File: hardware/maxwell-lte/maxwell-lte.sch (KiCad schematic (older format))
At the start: 25 parts, among them J1 LTE, J2 GPS, J3 Input, J4 SIM_Card, U1 MIC5209-ADJ, U2 SIM7000A, U3 TXB0104D, U4 SC16IS750IPW, Y1 Crystal

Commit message: Rev 1.1.
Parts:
- removed C8, C9: 220u / TAJC227K006RNJ, coddingtonbear:CP_Tantalum_Case-C_EIA-6032-28_Milling, symbol Device:CP
- removed R4, R5, R6: 22, coddingtonbear:0805_Milling, symbol Device:R
- added D1: 1N4148W, coddingtonbear:D_SOD-123_LargePads, symbol Device:D
- added R7: 1k, coddingtonbear:0805_Milling, symbol Device:R
- added R8: 3.6k, coddingtonbear:0805_Milling, symbol Device:R
- C7: value 220u / TAJC227K006RNJ -> 0.1 / FG0H104ZF; footprint coddingtonbear:CP_Tantalum_Case-C_EIA-6032-28_Milling -> Capacitor_THT:C_Disc_D11.0mm_W5.0mm_P5.00mm
- J1, J2: footprint Connector_Coaxial:SMA_Amphenol_132134_Vertical -> coddingtonbear:SMA_Amphenol_132134_Vertical_Largepads
- U1: footprint Package_SO:SOIC-8_3.9x4.9mm_P1.27mm -> coddingtonbear:SOIC-8_3.9x4.9mm_P1.27mm_LargePads
- U3: footprint Package_SO:SOIC-14_3.9x8.7mm_P1.27mm -> coddingtonbear:SOIC-14_3.9x8.7mm_P1.27mm_LargePads
- U4: footprint Package_SO:TSSOP-24_4.4x7.8mm_P0.65mm -> coddingtonbear:TSSOP-24_4.4x7.8mm_P0.65mm_LargePads
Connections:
- net +3V3: now also R7.1
- net GND: now also R8.2
- net EN_OUTPUT: now reaches U4.21 (DTRA/)
- net EN_OUTPUT: now also U3.8 (OE)
- net at U2.31 (SIM_DATA): now also J4.7 (I/O)
- net at U2.32 (SIM_CLK): now also J4.3 (CLK)
- net at U2.33 (SIM_RST): now also J4.2 (RST)
- net VDD_EXT renamed +1V8
- net +1V8: now also D1.1 (K); no longer U3.8 (OE)
- new net: D1.2 (A), R7.2, R8.1
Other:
- moved on the sheet: J1
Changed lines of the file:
@@
 EESchema Schematic File Version 4
 LIBS:maxwell-lte-cache
-EELAYER 26 0
+EELAYER 28 0
 EELAYER END
 $Descr A4 11693 8268
@@
 L Connector:Conn_Coaxial J1
 U 1 1 5BB94EB6
-P 1900 1750
-F 0 "J1" H 2000 1634 50  0000 L CNN
-F 1 "LTE" H 2000 1725 50  0000 L CNN
-F 2 "Connector_Coaxial:SMA_Amphenol_132134_Vertical" H 1900 1750 50  0001 C CNN
-F 3 " ~" H 1900 1750 50  0001 C CNN
-	1    1900 1750
+P 1850 1400
+F 0 "J1" H 1950 1284 50  0000 L CNN
+F 1 "LTE" H 1950 1375 50  0000 L CNN
+F 2 "coddingtonbear:SMA_Amphenol_132134_Vertical_Largepads" H 1850 1400 50  0001 C CNN
+F 3 " ~" H 1850 1400 50  0001 C CNN
+	1    1850 1400
 	-1   0    0    1
 $EndComp
@@
 F 0 "J2" H 2000 2184 50  0000 L CNN
 F 1 "GPS" H 2000 2275 50  0000 L CNN
-F 2 "Connector_Coaxial:SMA_Amphenol_132134_Vertical" H 1900 2300 50  0001 C CNN
+F 2 "coddingtonbear:SMA_Amphenol_132134_Vertical_Largepads" H 1900 2300 50  0001 C CNN
 F 3 " ~" H 1900 2300 50  0001 C CNN
 	1    1900 2300
@@
 	1    0    0    -1
 $EndComp
-Wire Wire Line
-	2100 1750 3600 1750
-Wire Wire Line
-	3600 1750 3600 2350
-Wire Wire Line
-	2100 2300 3500 2300
 Wire Wire Line
 	3500 2300 3500 2350
@@
 F 0 "U4" H 9200 1413 60  0000 C CNN
 F 1 "SC16IS750IPW" H 9200 1519 60  0000 C CNN
-F 2 "Package_SO:TSSOP-24_4.4x7.8mm_P0.65mm" H 9200 3550 60  0001 C CNN
+F 2 "coddingtonbear:TSSOP-24_4.4x7.8mm_P0.65mm_LargePads" H 9200 3550 60  0001 C CNN
 F 3 "" H 9200 3550 60  0000 C CNN
 	1    9200 2600
@@
 F 0 "U3" H 7450 2264 50  0000 C CNN
 F 1 "TXB0104D" H 7150 2350 50  0000 C CNN
-F 2 "Package_SO:SOIC-14_3.9x8.7mm_P1.27mm" H 7450 2300 50  0001 C CNN
+F 2 "coddingtonbear:SOIC-14_3.9x8.7mm_P1.27mm_LargePads" H 7450 2300 50  0001 C CNN
 F 3 "http://www.ti.com/lit/ds/symlink/txb0104.pdf" H 7560 3145 50  0001 C CNN
 	1    7450 3050
@@
 F 0 "U1" H 3300 6887 60  0000 C CNN
 F 1 "MIC5209-ADJ" H 3300 6781 60  0000 C CNN
-F 2 "Package_SO:SOIC-8_3.9x4.9mm_P1.27mm" H 3300 6400 60  0001 C CNN
+F 2 "coddingtonbear:SOIC-8_3.9x4.9mm_P1.27mm_LargePads" H 3300 6400 60  0001 C CNN
 F 3 "" H 3300 6400 60  0001 C CNN
 	1    3300 6400
@@
 $EndComp
 Wire Wire Line
-	4800 2350 4800 1850
-Wire Wire Line
-	4800 1850 6450 1850
-Wire Wire Line
-	7350 1850 7350 2250
-Wire Wire Line
 	7350 2250 7350 2350
-Connection ~ 7350 2250
 Wire Wire Line
 	7550 2250 7550 2350
@@
 L power:GND #PWR0117
 U 1 1 5BBEDF0C
-P 1400 1550
-F 0 "#PWR0117" H 1400 1300 50  0001 C CNN
-F 1 "GND" H 1405 1377 50  0000 C CNN
-F 2 "" H 1400 1550 50  0001 C CNN
-F 3 "" H 1400 1550 50  0001 C CNN
-	1    1400 1550
+P 1350 1200
+F 0 "#PWR0117" H 1350 950 50  0001 C CNN
+F 1 "GND" H 1355 1027 50  0000 C CNN
+F 2 "" H 1350 1200 50  0001 C CNN
+F 3 "" H 1350 1200 50  0001 C CNN
+	1    1350 1200
 	1    0    0    -1
 $EndComp
@@
 $EndComp
 Wire Wire Line
-	1900 1550 1400 1550
+	1850 1200 1350 1200
 Wire Wire Line
 	1900 2100 1350 2100
@@
 Text Label 6600 3150 0    50   ~ 0
 LTE_DTR_L
-Text Label 6000 1850 0    50   ~ 0
-VDD_EXT
-Text Label 2600 1750 0    50   ~ 0
+Text Label 2550 1400 0    50   ~ 0
 LTE_ANT
 Text Label 2600 2300 0    50   ~ 0
@@
 	-1   0    0    1
 $EndComp
-$Comp
-L Device:CP C8
-U 1 1 5BC2DBF3
-P 4300 1600
-F 0 "C8" V 4555 1600 50  0000 C CNN
-F 1 "220u / TAJC227K006RNJ" V 4464 1600 50  0000 C CNN
-F 2 "coddingtonbear:CP_Tantalum_Case-C_EIA-6032-28_Milling" H 4338 1450 50  0001 C CNN
-F 3 "~" H 4300 1600 50  0001 C CNN
-	1    4300 1600
-	0    -1   -1   0
-$EndComp
-Wire Wire Line
-	4150 1200 4150 1600
-Connection ~ 4150 1600
-$Comp
-L Device:CP C7
-U 1 1 5BC3EBE6
-P 4300 1200
-F 0 "C7" V 4555 1200 50  0000 C CNN
-F 1 "220u / TAJC227K006RNJ" V 4464 1200 50  0000 C CNN
-F 2 "coddingtonbear:CP_Tantalum_Case-C_EIA-6032-28_Milling" H 4338 1050 50  0001 C CNN
-F 3 "~" H 4300 1200 50  0001 C CNN
-	1    4300 1200
-	0    -1   -1   0
-$EndComp
-Wire Wire Line
-	4150 1600 4150 2000
-$Comp
-L Device:CP C9
-U 1 1 5BC3EC4C
-P 4300 2000
-F 0 "C9" V 4555 2000 50  0000 C CNN
-F 1 "220u / TAJC227K006RNJ" V 4464 2000 50  0000 C CNN
-F 2 "coddingtonbear:CP_Tantalum_Case-C_EIA-6032-28_Milling" H 4338 1850 50  0001 C CNN
-F 3 "~" H 4300 2000 50  0001 C CNN
-	1    4300 2000
-	0    -1   -1   0
-$EndComp
 Wire Wire Line
 	4150 1200 3750 1200
-Connection ~ 4150 1200
-Wire Wire Line
-	3200 900  3200 1200
-Wire Wire Line
-	3200 1200 3750 1200
-Connection ~ 3750 1200
-Connection ~ 4150 2000
-Wire Wire Line
-	4150 2000 4150 2200
 $Comp
 L power:GND #PWR0120
@@
 $EndComp
 Wire Wire Line
-	4450 2100 4450 2000
-Wire Wire Line
-	4450 2000 4450 1600
-Connection ~ 4450 2000
-Wire Wire Line
-	4450 1600 4450 1200
-Connection ~ 4450 1600
-Wire Wire Line
-	4450 1200 4450 900
-Wire Wire Line
 	4450 900  3750 900
-Connection ~ 4450 1200
 $Comp
 L Device:C C10
@@
 Wire Wire Line
 	6050 3850 6500 3850
-$Comp
-L Device:R R5
-U 1 1 5BC5FF4A
-P 6000 4250
-F 0 "R5" H 6070 4296 50  0000 L CNN
-F 1 "22" H 6070 4205 50  0000 L CNN
-F 2 "coddingtonbear:0805_Milling" V 5930 4250 50  0001 C CNN
-F 3 "~" H 6000 4250 50  0001 C CNN
-	1    6000 4250
-	0    1    1    0
-$EndComp
 Wire Wire Line
 	5800 4150 5800 4550
@@
 	5800 4150 6050 4150
 $Comp
-L Device:R R6
-U 1 1 5BC6524B
-P 6000 4350
-F 0 "R6" H 6070 4396 50  0000 L CNN
-F 1 "22" H 6070 4305 50  0000 L CNN
-F 2 "coddingtonbear:0805_Milling" V 5930 4350 50  0001 C CNN
-F 3 "~" H 6000 4350 50  0001 C CNN
-	1    6000 4350
-	0    1    1    0
-$EndComp
-$Comp
-L Device:R R4
-U 1 1 5BC6528B
-P 5900 4600
-F 0 "R4" H 5970 4646 50  0000 L CNN
-F 1 "22" H 5970 4555 50  0000 L CNN
-F 2 "coddingtonbear:0805_Milling" V 5830 4600 50  0001 C CNN
-F 3 "~" H 5900 4600 50  0001 C CNN
-	1    5900 4600
+L power:+3V3 #PWR0122
+U 1 1 5BC55B46
+P 5500 1450
+F 0 "#PWR0122" H 5500 1300 50  0001 C CNN
+F 1 "+3V3" H 5515 1623 50  0000 C CNN
+F 2 "" H 5500 1450 50  0001 C CNN
+F 3 "" H 5500 1450 50  0001 C CNN
+	1    5500 1450
+	1    0    0    -1
+$EndComp
+$Comp
+L Device:R R7
+U 1 1 5BC58077
+P 5500 1600
+F 0 "R7" H 5570 1646 50  0000 L CNN
+F 1 "1k" H 5570 1555 50  0000 L CNN
+F 2 "coddingtonbear:0805_Milling" V 5430 1600 50  0001 C CNN
+F 3 "~" H 5500 1600 50  0001 C CNN
+	1    5500 1600
+	1    0    0    -1
+$EndComp
+$Comp
+L Device:R R8
+U 1 1 5BC5A95F
+P 5500 1900
+F 0 "R8" H 5570 1946 50  0000 L CNN
+F 1 "3.6k" H 5570 1855 50  0000 L CNN
+F 2 "coddingtonbear:0805_Milling" V 5430 1900 50  0001 C CNN
+F 3 "~" H 5500 1900 50  0001 C CNN
+	1    5500 1900
+	1    0    0    -1
+$EndComp
+$Comp
+L power:GND #PWR0123
+U 1 1 5BC5C791
+P 5500 2050
+F 0 "#PWR0123" H 5500 1800 50  0001 C CNN
+F 1 "GND" H 5505 1877 50  0000 C CNN
+F 2 "" H 5500 2050 50  0001 C CNN
+F 3 "" H 5500 2050 50  0001 C CNN
+	1    5500 2050
+	1    0    0    -1
+$EndComp
+Wire Wire Line
+	7350 1750 7350 2250
+Connection ~ 7350 2250
+$Comp
+L power:+1V8 #PWR0124
+U 1 1 5BC6DF49
+P 6650 1750
+F 0 "#PWR0124" H 6650 1600 50  0001 C CNN
+F 1 "+1V8" H 6665 1923 50  0000 C CNN
+F 2 "" H 6650 1750 50  0001 C CNN
+F 3 "" H 6650 1750 50  0001 C CNN
+	1    6650 1750
+	1    0    0    -1
+$EndComp
+Wire Wire Line
+	6650 1750 7350 1750
+Text GLabel 6700 2500 1    50   Input ~ 0
+EN_OUTPUT
+Wire Wire Line
+	8300 2550 8300 2900
+Wire Wire Line
+	8300 2900 8400 2900
+Wire Wire Line
+	6700 2500 6700 2550
+Wire Wire Line
+	6700 2550 7050 2550
+Text GLabel 8300 2550 1    50   Output ~ 0
+EN_OUTPUT
+Wire Wire Line
+	5750 4250 6200 4250
+Wire Wire Line
+	5750 4350 6200 4350
+Wire Wire Line
+	6200 4650 5900 4650
+Wire Wire Line
+	5900 4450 5900 4650
+Wire Wire Line
+	3200 900  3200 1200
+Wire Wire Line
+	3200 1200 3750 1200
+Connection ~ 3750 1200
+Wire Wire Line
+	2050 1400 3600 1400
+Wire Wire Line
+	3600 1400 3600 2350
+Wire Wire Line
+	2100 2300 3500 2300
+Wire Wire Line
+	4150 1200 4150 1650
+Wire Wire Line
+	4450 900  4450 1650
+$Comp
+L Device:CP C7
+U 1 1 5BCFB050
+P 4300 1650
+F 0 "C7" V 4555 1650 50  0000 C CNN
+F 1 "0.1 / FG0H104ZF" V 4464 1650 50  0000 C CNN
+F 2 "Capacitor_THT:C_Disc_D11.0mm_W5.0mm_P5.00mm" H 4338 1500 50  0001 C CNN
+F 3 "~" H 4300 1650 50  0001 C CNN
+	1    4300 1650
+	0    -1   -1   0
+$EndComp
+Connection ~ 4150 1650
+Wire Wire Line
+	4150 1650 4150 2200
+Connection ~ 4450 1650
+Wire Wire Line
+	4450 1650 4450 2100
+$Comp
+L Device:D D1
+U 1 1 5BDAAFFC
+P 5900 1750
+F 0 "D1" H 5900 1534 50  0000 C CNN
+F 1 "1N4148W" H 5900 1625 50  0000 C CNN
+F 2 "coddingtonbear:D_SOD-123_LargePads" H 5900 1750 50  0001 C CNN
+F 3 "~" H 5900 1750 50  0001 C CNN
+	1    5900 1750
 	-1   0    0    1
 $EndComp
 Wire Wire Line
-	5850 4250 5750 4250
-Wire Wire Line
-	5750 4350 5850 4350
-Wire Wire Line
-	6150 4250 6200 4250
-Wire Wire Line
-	6200 4350 6150 4350
-Wire Wire Line
-	5900 4750 6200 4750
-Wire Wire Line
-	6200 4750 6200 4650
-Wire Wire Line
-	7050 2550 6450 2550
-Wire Wire Line
-	6450 2550 6450 1850
-Connection ~ 6450 1850
-Wire Wire Line
-	6450 1850 7350 1850
+	5750 1750 5500 1750
+Connection ~ 5500 1750
+Wire Wire Line
+	4800 2350 6050 2350
+Wire Wire Line
+	6050 2350 6050 1750
+Wire Wire Line
+	6650 1750 6050 1750
+Connection ~ 6650 1750
+Connection ~ 6050 1750
 $EndSCHEMATC

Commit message: Give a direct link to PWRKEY from the level converter in case my bootstrapping strategy is unworkable.
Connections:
- net PWRKEY: now also U4.20 (DSRA/)
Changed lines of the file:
@@
 Connection ~ 6650 1750
 Connection ~ 6050 1750
+Text GLabel 8300 3500 0    50   Output ~ 0
+PWRKEY
+Wire Wire Line
+	8400 3000 8300 3000
+Wire Wire Line
+	8300 3000 8300 3500
 $EndSCHEMATC

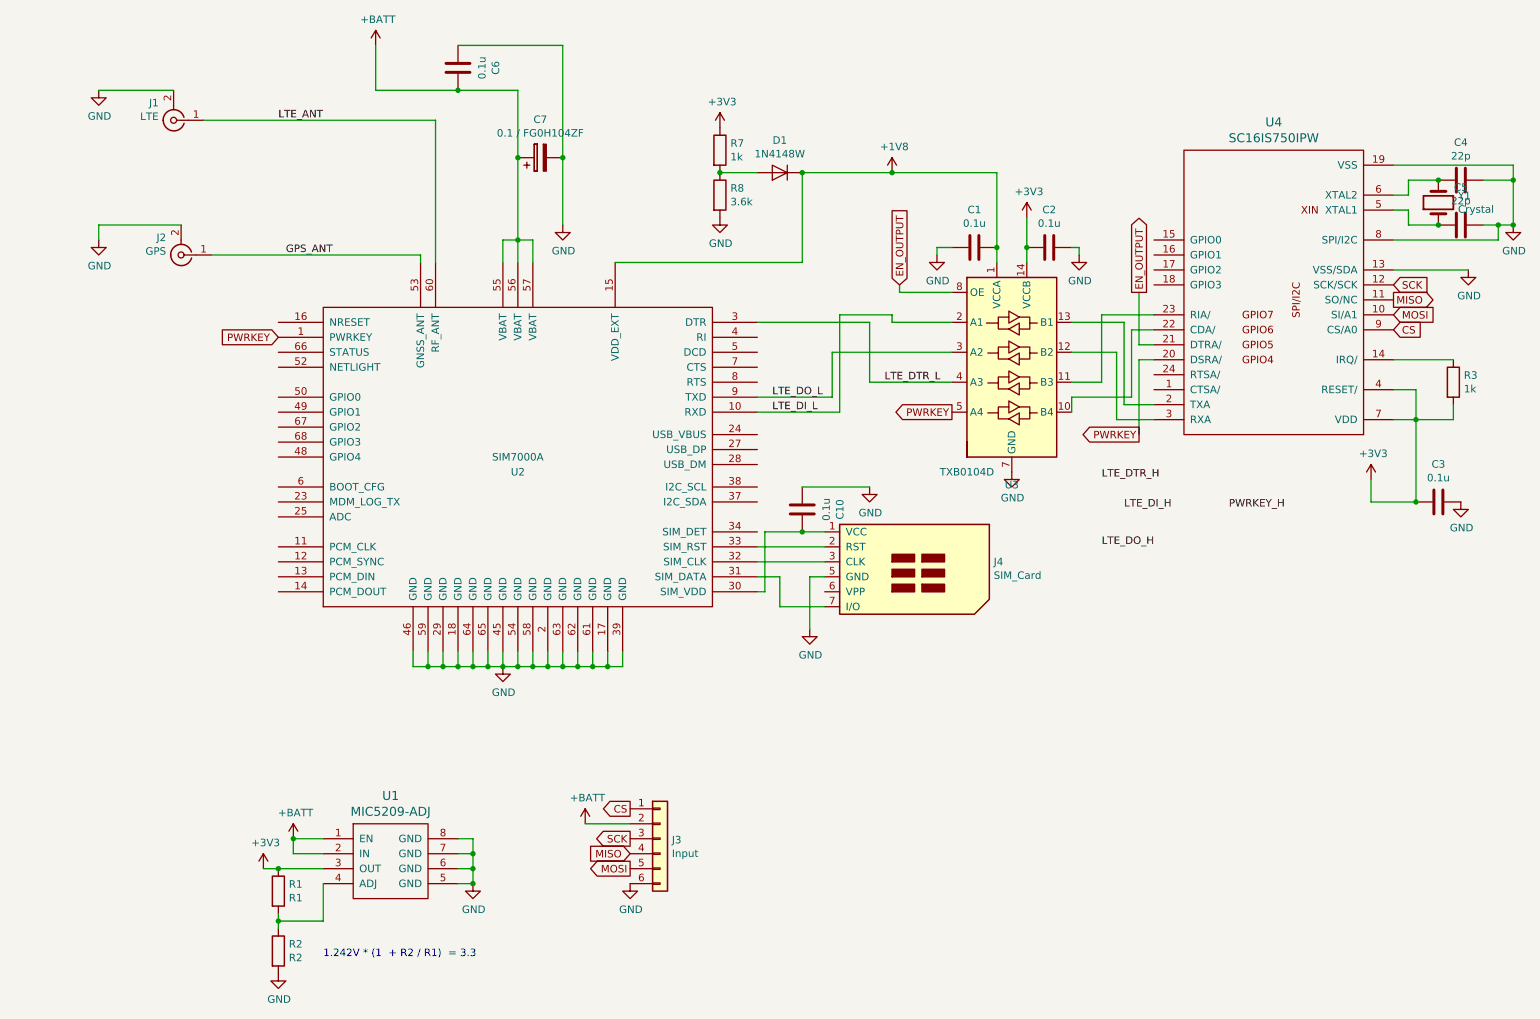
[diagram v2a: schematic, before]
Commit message: Updating to v1.4; adds output capacitor to onboard regulator; adds status input to level shifter.
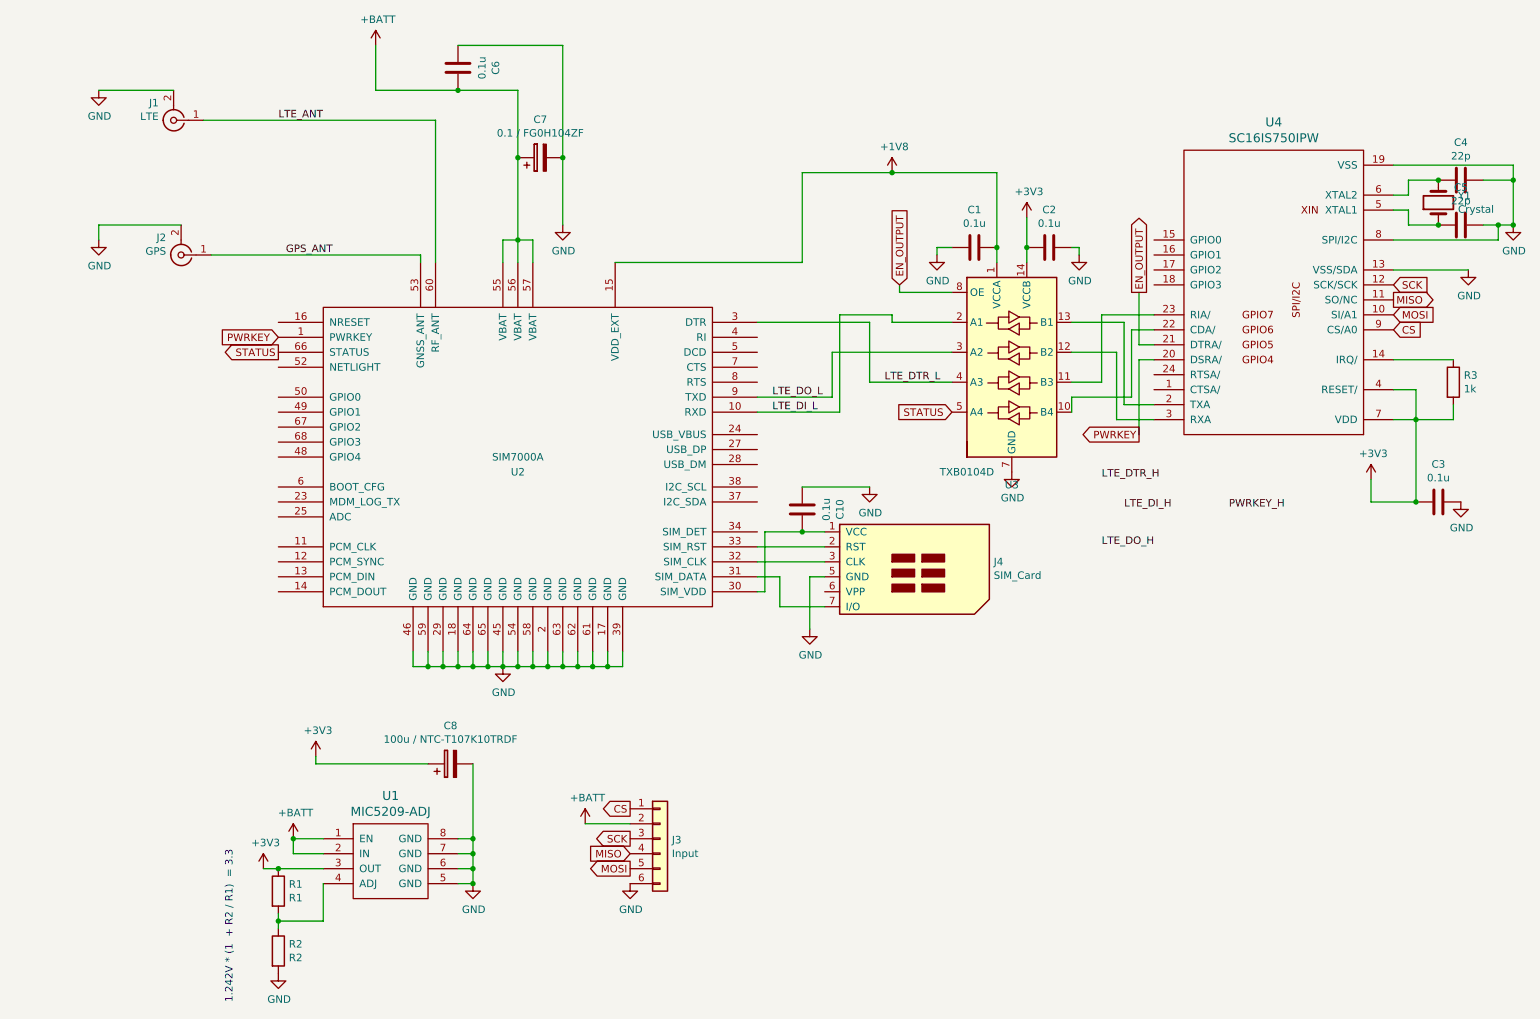
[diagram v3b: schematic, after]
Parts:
- removed D1: 1N4148W, coddingtonbear:D_SOD-123_LargePads, symbol Device:D
- removed R7: 1k, coddingtonbear:0805_Milling, symbol Device:R
- removed R8: 3.6k, coddingtonbear:0805_Milling, symbol Device:R
- added C8: 100u / NTC-T107K10TRDF, coddingtonbear:CP_Tantalum_Case-D_EIA-7343-31_Milling, symbol Device:CP
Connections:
- net +3V3: now also C8.1
- net GND: now also C8.2
- net PWRKEY: no longer U3.5 (A4)
- net STATUS: now reaches U2.66 (STATUS)
- net STATUS: now also U3.5 (A4)
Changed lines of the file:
@@
 Wire Wire Line
 	3850 6400 3850 6500
-Wire Wire Line
-	3750 6500 3850 6500
 Connection ~ 3850 6500
 $Comp
@@
 Wire Wire Line
 	6100 4450 6100 4800
-Text GLabel 7050 3350 0    50   Output ~ 0
-PWRKEY
 Text GLabel 2550 2850 0    50   Input ~ 0
 PWRKEY
@@
 Wire Wire Line
 	2550 6750 2550 6800
-Text Notes 2850 7000 0    50   ~ 0
+Text Notes 2250 7300 1    50   ~ 0
 1.242V * (1  + R2 / R1)  = 3.3
 Text Label 5850 3350 0    50   ~ 0
@@
 Wire Wire Line
 	5800 4150 6050 4150
-$Comp
-L power:+3V3 #PWR0122
-U 1 1 5BC55B46
-P 5500 1450
-F 0 "#PWR0122" H 5500 1300 50  0001 C CNN
-F 1 "+3V3" H 5515 1623 50  0000 C CNN
-F 2 "" H 5500 1450 50  0001 C CNN
-F 3 "" H 5500 1450 50  0001 C CNN
-	1    5500 1450
-	1    0    0    -1
-$EndComp
-$Comp
-L Device:R R7
-U 1 1 5BC58077
-P 5500 1600
-F 0 "R7" H 5570 1646 50  0000 L CNN
-F 1 "1k" H 5570 1555 50  0000 L CNN
-F 2 "coddingtonbear:0805_Milling" V 5430 1600 50  0001 C CNN
-F 3 "~" H 5500 1600 50  0001 C CNN
-	1    5500 1600
-	1    0    0    -1
-$EndComp
-$Comp
-L Device:R R8
-U 1 1 5BC5A95F
-P 5500 1900
-F 0 "R8" H 5570 1946 50  0000 L CNN
-F 1 "3.6k" H 5570 1855 50  0000 L CNN
-F 2 "coddingtonbear:0805_Milling" V 5430 1900 50  0001 C CNN
-F 3 "~" H 5500 1900 50  0001 C CNN
-	1    5500 1900
-	1    0    0    -1
-$EndComp
-$Comp
-L power:GND #PWR0123
-U 1 1 5BC5C791
-P 5500 2050
-F 0 "#PWR0123" H 5500 1800 50  0001 C CNN
-F 1 "GND" H 5505 1877 50  0000 C CNN
-F 2 "" H 5500 2050 50  0001 C CNN
-F 3 "" H 5500 2050 50  0001 C CNN
-	1    5500 2050
-	1    0    0    -1
-$EndComp
 Wire Wire Line
 	7350 1750 7350 2250
@@
 Wire Wire Line
 	4450 1650 4450 2100
-$Comp
-L Device:D D1
-U 1 1 5BDAAFFC
-P 5900 1750
-F 0 "D1" H 5900 1534 50  0000 C CNN
-F 1 "1N4148W" H 5900 1625 50  0000 C CNN
-F 2 "coddingtonbear:D_SOD-123_LargePads" H 5900 1750 50  0001 C CNN
-F 3 "~" H 5900 1750 50  0001 C CNN
-	1    5900 1750
-	-1   0    0    1
-$EndComp
-Wire Wire Line
-	5750 1750 5500 1750
-Connection ~ 5500 1750
 Wire Wire Line
 	4800 2350 6050 2350
@@
 	6650 1750 6050 1750
 Connection ~ 6650 1750
-Connection ~ 6050 1750
 Text GLabel 8300 3500 0    50   Output ~ 0
 PWRKEY
@@
 Wire Wire Line
 	8300 3000 8300 3500
+Text GLabel 2550 2950 0    50   Output ~ 0
+STATUS
+Text GLabel 7050 3350 0    50   Input ~ 0
+STATUS
+$Comp
+L Device:CP C8
+U 1 1 5BC749F4
+P 3700 5700
+F 0 "C8" V 3955 5700 50  0000 C CNN
+F 1 "100u / NTC-T107K10TRDF" V 3864 5700 50  0000 C CNN
+F 2 "coddingtonbear:CP_Tantalum_Case-D_EIA-7343-31_Milling" H 3738 5550 50  0001 C CNN
+F 3 "~" H 3700 5700 50  0001 C CNN
+	1    3700 5700
+	0    -1   -1   0
+$EndComp
+$Comp
+L power:+3V3 #PWR?
+U 1 1 5BCAD008
+P 2800 5650
+F 0 "#PWR?" H 2800 5500 50  0001 C CNN
+F 1 "+3V3" H 2815 5823 50  0000 C CNN
+F 2 "" H 2800 5650 50  0001 C CNN
+F 3 "" H 2800 5650 50  0001 C CNN
+	1    2800 5650
+	1    0    0    -1
+$EndComp
+Wire Wire Line
+	3750 6500 3850 6500
+Wire Wire Line
+	3850 5700 3850 6200
+Connection ~ 3850 6200
+Wire Wire Line
+	3550 5700 2800 5700
+Wire Wire Line
+	2800 5700 2800 5650
 $EndSCHEMATC

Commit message: Finalizing v1.4.
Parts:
- added C11, C9: 220u / TAJC227K006RNJ, coddingtonbear:CP_Tantalum_Case-C_EIA-6032-28_Milling, symbol Device:CP
- added J10, J11, J12, J13, J5, J6, J7, J8, J9, J? (x4): Stitching, coddingtonbear:Thermal_Relief_Via_Milling, symbol Connector_Generic:Conn_01x01
- added J?: Stiching, coddingtonbear:Thermal_Relief_Via_Milling, symbol Connector_Generic:Conn_01x01
- added R4: 10k, coddingtonbear:0805_Milling, symbol Device:R
- C7: value 0.1 / FG0H104ZF -> 220u / TAJC227K006RNJ; footprint Capacitor_THT:C_Disc_D11.0mm_W5.0mm_P5.00mm -> coddingtonbear:CP_Tantalum_Case-C_EIA-6032-28_Milling
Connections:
- net +BATT: now also C11.1, C9.1
- net GND: now also C11.2, C9.2, J10.1 (Pin_1), J11.1 (Pin_1), J12.1 (Pin_1), J13.1 (Pin_1), J5.1 (Pin_1), J6.1 (Pin_1), J7.1 (Pin_1), J8.1 (Pin_1), J9.1 (Pin_1), J?.1 (Pin_1), J?.1 (Pin_1), J?.1 (Pin_1), J?.1 (Pin_1), J?.1 (Pin_1), R4.2
- net LTE_DI_H: now also U3.13 (B1), U4.2 (TXA)
- net LTE_DO_H: now also U3.12 (B2), U4.3 (RXA)
- net LTE_DTR_H: now also U3.11 (B3), U4.23 (RIA/)
- net STATUS_H: now reaches U3.10 (B4), U4.22 (CDA/)
- net STATUS_H: now also R4.1
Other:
- note added: "Via RF Guard Stitching"
